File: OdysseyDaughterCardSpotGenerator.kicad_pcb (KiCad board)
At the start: 2 copper layers, 37.1 x 46.6 mm, 20 parts, among them Q1 2N3904, Q2 2N3904, Q3 BC547C, Q4 2N3904, X1 OdysseyDaughterCard

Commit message: 1.0 add port for emulator team
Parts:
- added J1: Conn_01x03, Connector_PinHeader_2.54mm:PinHeader_1x03_P2.54mm_Vertical, F.Cu at (156.7, 120.9)
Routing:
- net /Card9: track 8.65 -> 62.4 mm
- net /Card2: track 8.22 -> 29.7 mm
- net GND: track 57.5 -> 65.2 mm
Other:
- board text added: "Daughter Card Spot Generator 9-29-2018 r1.0 University of Pittsburgh Odyssey Restoration Project"
- board text removed: "Daughter Card Spot Generator 6-3-2018 r0.1 University of Pittsburgh Odyssey Restoration Project"
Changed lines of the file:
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@@
-(kicad_pcb (version 20171130) (host pcbnew "(2017-12-21 revision 23d71cfa9)-makepkg")
+(kicad_pcb (version 20171130) (host pcbnew "(5.0.0)")
   (general
     (thickness 1.6)
     (drawings 13)
-    (tracks 104)
+    (tracks 115)
     (zones 0)
-    (modules 20)
+    (modules 21)
     (nets 17)
   )
@@
   (title_block
     (title "Odyssey Daughter Card Spot Generator")
-    (date 2018-06-03)
-    (rev 0.1)
+    (date 2018-09-29)
+    (rev 1.0)
     (company "University of Pittsburgh - Odyssey Restoration Project")
     (comment 1 "Levi Burner")
@@
     (pcbplotparams
       (layerselection 0x010f0_ffffffff)
-      (usegerberextensions true)
+      (usegerberextensions false)
       (usegerberattributes false)
       (usegerberadvancedattributes false)
@@
       (hpglpennumber 1)
       (hpglpenspeed 20)
-      (hpglpendiameter 15)
+      (hpglpendiameter 15.000000)
       (psnegative false)
       (psa4output false)
@@
       (drillshape 0)
       (scaleselection 1)
-      (outputdirectory gerbers/))
+      (outputdirectory "gerbers/"))
   )
   (net 0 "")
@@
     )
   )
+  (module Connector_PinHeader_2.54mm:PinHeader_1x03_P2.54mm_Vertical (layer F.Cu)
+    (at 156.718 120.904 180)
+    (descr "Through hole straight pin header, 1x03, 2.54mm pitch, single row")
+    (tags "Through hole pin header THT 1x03 2.54mm single row")
+    (fp_text reference J1 (at 0 -2.33 180) (layer F.SilkS)
+      (effects (font (size 1 1) (thickness 0.15)))
+    )
+    (fp_text value Conn_01x03 (at 0 7.41 180) (layer F.Fab)
+      (effects (font (size 1 1) (thickness 0.15)))
+    )
+    (fp_line (start -0.635 -1.27) (end 1.27 -1.27) (layer F.Fab) (width 0.1))
+    (fp_line (start 1.27 -1.27) (end 1.27 6.35) (layer F.Fab) (width 0.1))
+    (fp_line (start 1.27 6.35) (end -1.27 6.35) (layer F.Fab) (width 0.1))
+    (fp_line (start -1.27 6.35) (end -1.27 -0.635) (layer F.Fab) (width 0.1))
+    (fp_line (start -1.27 -0.635) (end -0.635 -1.27) (layer F.Fab) (width 0.1))
+    (fp_line (start -1.33 6.41) (end 1.33 6.41) (layer F.SilkS) (width 0.12))
+    (fp_line (start -1.33 1.27) (end -1.33 6.41) (layer F.SilkS) (width 0.12))
+    (fp_line (start 1.33 1.27) (end 1.33 6.41) (layer F.SilkS) (width 0.12))
+    (fp_line (start -1.33 1.27) (end 1.33 1.27) (layer F.SilkS) (width 0.12))
+    (fp_line (start -1.33 0) (end -1.33 -1.33) (layer F.SilkS) (width 0.12))
+    (fp_line (start -1.33 -1.33) (end 0 -1.33) (layer F.SilkS) (width 0.12))
+    (fp_line (start -1.8 -1.8) (end -1.8 6.85) (layer F.CrtYd) (width 0.05))
+    (fp_line (start -1.8 6.85) (end 1.8 6.85) (layer F.CrtYd) (width 0.05))
+    (fp_line (start 1.8 6.85) (end 1.8 -1.8) (layer F.CrtYd) (width 0.05))
+    (fp_line (start 1.8 -1.8) (end -1.8 -1.8) (layer F.CrtYd) (width 0.05))
+    (fp_text user %R (at 0 2.54 270) (layer F.Fab)
+      (effects (font (size 1 1) (thickness 0.15)))
+    )
+    (pad 1 thru_hole rect (at 0 0 180) (size 1.7 1.7) (drill 1) (layers *.Cu *.Mask)
+      (net 16 /Card2))
+    (pad 2 thru_hole oval (at 0 2.54 180) (size 1.7 1.7) (drill 1) (layers *.Cu *.Mask)
+      (net 13 /Card9))
+    (pad 3 thru_hole oval (at 0 5.08 180) (size 1.7 1.7) (drill 1) (layers *.Cu *.Mask)
+      (net 11 GND))
+    (model ${KISYS3DMOD}/Connector_PinHeader_2.54mm.3dshapes/PinHeader_1x03_P2.54mm_Vertical.wrl
+      (at (xyz 0 0 0))
+      (scale (xyz 1 1 1))
+      (rotate (xyz 0 0 0))
+    )
+  )
   (gr_line (start 159.512 77.7) (end 159.512 124.3) (layer Edge.Cuts) (width 0.15))
   (gr_line (start 126.175 77.7) (end 122.425 77.7) (layer Edge.Cuts) (width 0.15))
@@
   (gr_line (start 126.175 124.3) (end 126.175 123.1) (layer Edge.Cuts) (width 0.15))
   (gr_line (start 122.425 124.3) (end 126.175 124.3) (layer Edge.Cuts) (width 0.15))
-  (gr_text "Daughter Card Spot Generator\n6-3-2018 r0.1\nUniversity of Pittsburgh\nOdyssey Restoration Project" (at 128.524 79.756 -90) (layer F.SilkS)
+  (gr_text "Daughter Card Spot Generator\n9-29-2018 r1.0\nUniversity of Pittsburgh\nOdyssey Restoration Project" (at 128.524 79.756 -90) (layer F.SilkS)
     (effects (font (size 1.2 1.2) (thickness 0.2)) (justify left))
   )
@@
   (segment (start 144.78 84.455) (end 144.78 80.812) (width 0.25) (layer B.Cu) (net 2))
   (segment (start 144.78 80.812) (end 144.78 80.772) (width 0.25) (layer B.Cu) (net 2))
-  (segment (start 148.8599 91.7823) (end 155.448 91.7823) (width 0.25) (layer F.Cu) (net 3))
-  (segment (start 145.9053 88.8277) (end 148.8599 91.7823) (width 0.25) (layer F.Cu) (net 3))
-  (segment (start 145.9053 88.265) (end 145.9053 88.8277) (width 0.25) (layer F.Cu) (net 3))
-  (segment (start 144.78 88.265) (end 145.9053 88.265) (width 0.25) (layer F.Cu) (net 3))
-  (segment (start 155.448 90.932) (end 155.448 91.7823) (width 0.25) (layer F.Cu) (net 3))
   (segment (start 155.956 92.2903) (end 155.956 99.608) (width 0.25) (layer B.Cu) (net 3))
   (segment (start 155.448 91.7823) (end 155.956 92.2903) (width 0.25) (layer B.Cu) (net 3))
   (segment (start 155.448 90.932) (end 155.448 91.7823) (width 0.25) (layer B.Cu) (net 3))
+  (segment (start 155.448 91.7823) (end 155.448 90.932) (width 0.25) (layer F.Cu) (net 3))
+  (segment (start 148.8599 91.7823) (end 155.448 91.7823) (width 0.25) (layer F.Cu) (net 3))
+  (segment (start 144.78 88.265) (end 145.3426 88.265) (width 0.25) (layer F.Cu) (net 3))
+  (segment (start 145.3426 88.265) (end 148.8599 91.7823) (width 0.25) (layer F.Cu) (net 3))
   (via (at 135.6058 94.3183) (size 0.8) (layers F.Cu B.Cu) (net 4))
   (segment (start 156.464 106.934) (end 155.3887 106.934) (width 0.25) (layer B.Cu) (net 4))
@@
   (segment (start 150.368 109.0543) (end 147.4501 111.9722) (width 0.25) (layer B.Cu) (net 11))
   (segment (start 150.368 108.204) (end 150.368 109.0543) (width 0.25) (layer B.Cu) (net 11))
+  (segment (start 156.718 108.458) (end 156.464 108.204) (width 0.25) (layer B.Cu) (net 11))
+  (segment (start 156.718 115.824) (end 156.718 108.458) (width 0.25) (layer B.Cu) (net 11))
   (segment (start 156.464 105.664) (end 150.368 105.664) (width 0.25) (layer F.Cu) (net 12))
   (segment (start 136.0347 104.4038) (end 134.8253 103.1944) (width 0.25) (layer B.Cu) (net 12))
@@
   (segment (start 137.16 84.455) (end 136.0092 84.455) (width 0.25) (layer B.Cu) (net 13))
   (segment (start 129 85.6389) (end 134.8253 85.6389) (width 0.25) (layer B.Cu) (net 13))
+  (segment (start 138.29137 84.455) (end 137.16 84.455) (width 0.25) (layer F.Cu) (net 13))
+  (segment (start 139.827 84.455) (end 138.29137 84.455) (width 0.25) (layer F.Cu) (net 13))
+  (segment (start 142.24 86.868) (end 139.827 84.455) (width 0.25) (layer F.Cu) (net 13))
+  (segment (start 157.893001 86.868) (end 142.24 86.868) (width 0.25) (layer F.Cu) (net 13))
+  (segment (start 156.718 118.364) (end 157.893001 117.188999) (width 0.25) (layer F.Cu) (net 13))
+  (segment (start 157.893001 117.188999) (end 157.893001 86.868) (width 0.25) (layer F.Cu) (net 13))
   (segment (start 137.16 88.265) (end 137.16 92.075) (width 0.25) (layer B.Cu) (net 14))
   (segment (start 137.16 92.075) (end 137.16 95.885) (width 0.25) (layer B.Cu) (net 14))
@@
   (segment (start 137.16 116.205) (end 134.9814 116.205) (width 0.25) (layer B.Cu) (net 16))
   (segment (start 129 116.3611) (end 134.8253 116.3611) (width 0.25) (layer B.Cu) (net 16))
+  (segment (start 155.618 120.904) (end 156.718 120.904) (width 0.25) (layer B.Cu) (net 16))
+  (segment (start 147.175001 120.904) (end 155.618 120.904) (width 0.25) (layer B.Cu) (net 16))
+  (segment (start 142.476001 116.205) (end 147.175001 120.904) (width 0.25) (layer B.Cu) (net 16))
+  (segment (start 137.16 116.205) (end 142.476001 116.205) (width 0.25) (layer B.Cu) (net 16))
 )

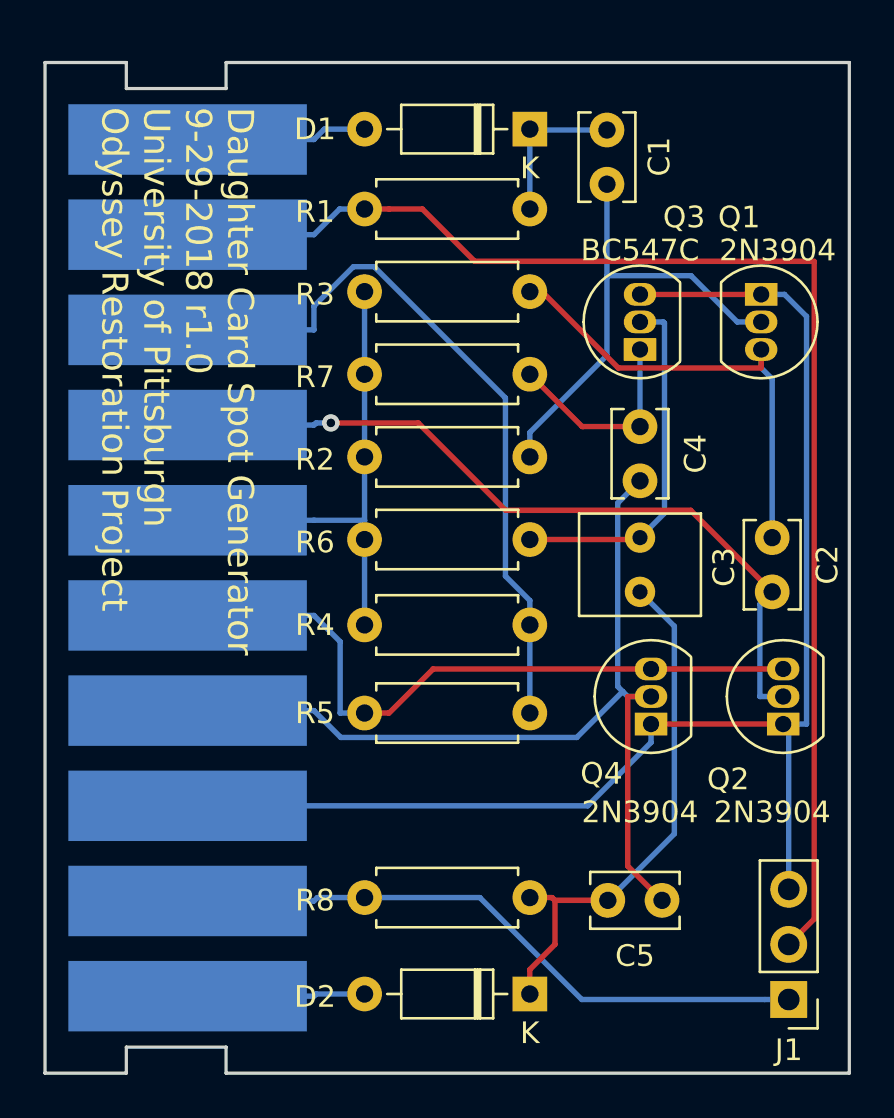
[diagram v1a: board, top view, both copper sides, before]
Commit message: R1.1 add header for extra player gen
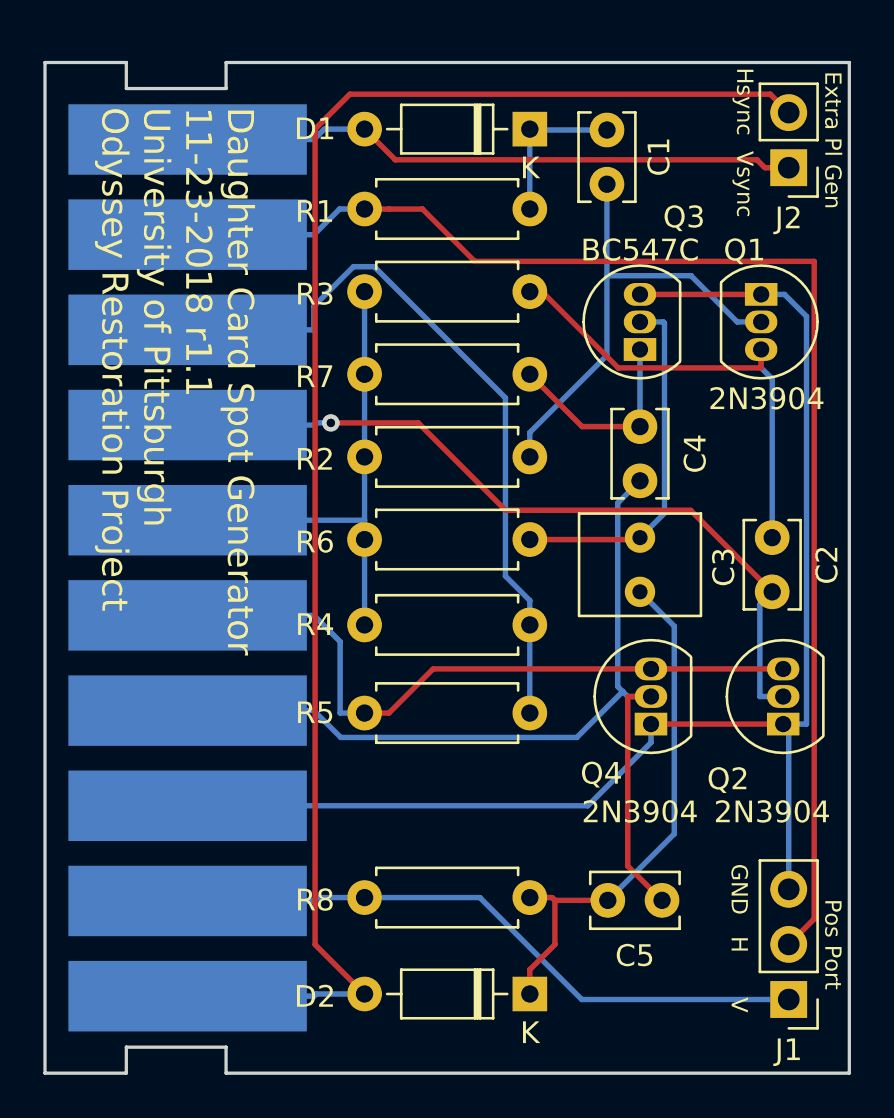
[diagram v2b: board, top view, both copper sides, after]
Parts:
- added J2: Conn_01x02, Connector_PinHeader_2.54mm:PinHeader_1x02_P2.54mm_Vertical, F.Cu at (156.7, 82.5)
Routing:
- net /Card1: track 8.20 -> 71.9 mm
- net /Card10: track 8.36 -> 28.7 mm
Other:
- board text added: "Daughter Card Spot Generator 11-23-2018 r1.1 University of Pittsburgh Odyssey Restoration Project"
- board text added: "Extra Pl Gen"
- board text added: "GND"
- board text added: "H"
- board text added: "Hsync"
- board text added: "Pos Port"
- board text added: "V"
- board text added: "Vsync"
- board text removed: "Daughter Card Spot Generator 9-29-2018 r1.0 University of Pittsburgh Odyssey Restoration Project"
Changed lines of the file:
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@@
-(kicad_pcb (version 20171130) (host pcbnew "(5.0.0)")
+(kicad_pcb (version 20171130) (host pcbnew "(5.0.1)-3")
   (general
     (thickness 1.6)
-    (drawings 13)
-    (tracks 115)
+    (drawings 20)
+    (tracks 124)
     (zones 0)
-    (modules 21)
+    (modules 22)
     (nets 17)
   )
@@
   (title_block
     (title "Odyssey Daughter Card Spot Generator")
-    (date 2018-09-29)
-    (rev 1.0)
+    (date 2018-11-23)
+    (rev 1.1)
     (company "University of Pittsburgh - Odyssey Restoration Project")
     (comment 1 "Levi Burner")
@@
     (pad_drill 0.762)
     (pad_to_mask_clearance 0.2)
+    (solder_mask_min_width 0.25)
     (aux_axis_origin 0 0)
     (visible_elements 7FFFFFFF)
@@
     (descr "TO-92 leads in-line, narrow, oval pads, drill 0.75mm (see NXP sot054_po.pdf)")
     (tags "to-92 sc-43 sc-43a sot54 PA33 transistor")
-    (fp_text reference Q1 (at -3.556 1.016) (layer F.SilkS)
-      (effects (font (size 1 1) (thickness 0.15)))
-    )
-    (fp_text value 2N3904 (at -2.032 -0.762) (layer F.SilkS)
+    (fp_text reference Q1 (at -2.032 0.762) (layer F.SilkS)
+      (effects (font (size 1 1) (thickness 0.15)))
+    )
+    (fp_text value 2N3904 (at 4.826 -0.254) (layer F.SilkS)
       (effects (font (size 1 1) (thickness 0.15)))
     )
@@
     )
   )
+  (module Connector_PinHeader_2.54mm:PinHeader_1x02_P2.54mm_Vertical (layer F.Cu)
+    (at 156.718 82.55 180)
+    (descr "Through hole straight pin header, 1x02, 2.54mm pitch, single row")
+    (tags "Through hole pin header THT 1x02 2.54mm single row")
+    (fp_text reference J2 (at 0 -2.33 180) (layer F.SilkS)
+      (effects (font (size 1 1) (thickness 0.15)))
+    )
+    (fp_text value Conn_01x02 (at 0 4.87 180) (layer F.Fab)
+      (effects (font (size 1 1) (thickness 0.15)))
+    )
+    (fp_line (start -0.635 -1.27) (end 1.27 -1.27) (layer F.Fab) (width 0.1))
+    (fp_line (start 1.27 -1.27) (end 1.27 3.81) (layer F.Fab) (width 0.1))
+    (fp_line (start 1.27 3.81) (end -1.27 3.81) (layer F.Fab) (width 0.1))
+    (fp_line (start -1.27 3.81) (end -1.27 -0.635) (layer F.Fab) (width 0.1))
+    (fp_line (start -1.27 -0.635) (end -0.635 -1.27) (layer F.Fab) (width 0.1))
+    (fp_line (start -1.33 3.87) (end 1.33 3.87) (layer F.SilkS) (width 0.12))
+    (fp_line (start -1.33 1.27) (end -1.33 3.87) (layer F.SilkS) (width 0.12))
+    (fp_line (start 1.33 1.27) (end 1.33 3.87) (layer F.SilkS) (width 0.12))
+    (fp_line (start -1.33 1.27) (end 1.33 1.27) (layer F.SilkS) (width 0.12))
+    (fp_line (start -1.33 0) (end -1.33 -1.33) (layer F.SilkS) (width 0.12))
+    (fp_line (start -1.33 -1.33) (end 0 -1.33) (layer F.SilkS) (width 0.12))
+    (fp_line (start -1.8 -1.8) (end -1.8 4.35) (layer F.CrtYd) (width 0.05))
+    (fp_line (start -1.8 4.35) (end 1.8 4.35) (layer F.CrtYd) (width 0.05))
+    (fp_line (start 1.8 4.35) (end 1.8 -1.8) (layer F.CrtYd) (width 0.05))
+    (fp_line (start 1.8 -1.8) (end -1.8 -1.8) (layer F.CrtYd) (width 0.05))
+    (fp_text user %R (at 0 1.27 270) (layer F.Fab)
+      (effects (font (size 1 1) (thickness 0.15)))
+    )
+    (pad 1 thru_hole rect (at 0 0 180) (size 1.7 1.7) (drill 1) (layers *.Cu *.Mask)
+      (net 9 /Card10))
+    (pad 2 thru_hole oval (at 0 2.54 180) (size 1.7 1.7) (drill 1) (layers *.Cu *.Mask)
+      (net 10 /Card1))
+    (model ${KISYS3DMOD}/Connector_PinHeader_2.54mm.3dshapes/PinHeader_1x02_P2.54mm_Vertical.wrl
+      (at (xyz 0 0 0))
+      (scale (xyz 1 1 1))
+      (rotate (xyz 0 0 0))
+    )
+  )
+  (gr_text Vsync (at 154.686 83.312 270) (layer F.SilkS)
+    (effects (font (size 0.75 0.75) (thickness 0.1)))
+  )
+  (gr_text Hsync (at 154.686 79.502 270) (layer F.SilkS)
+    (effects (font (size 0.75 0.75) (thickness 0.1)))
+  )
+  (gr_text "Extra Pl Gen" (at 158.75 81.28 270) (layer F.SilkS)
+    (effects (font (size 0.75 0.75) (thickness 0.1)))
+  )
+  (gr_text V (at 154.432 121.158 270) (layer F.SilkS)
+    (effects (font (size 0.75 0.75) (thickness 0.1)))
+  )
+  (gr_text H (at 154.432 118.364 270) (layer F.SilkS)
+    (effects (font (size 0.75 0.75) (thickness 0.1)))
+  )
+  (gr_text GND (at 154.432 115.824 270) (layer F.SilkS)
+    (effects (font (size 0.75 0.75) (thickness 0.1)))
+  )
+  (gr_text "Pos Port" (at 158.75 118.364 270) (layer F.SilkS)
+    (effects (font (size 0.75 0.75) (thickness 0.1)))
+  )
   (gr_line (start 159.512 77.7) (end 159.512 124.3) (layer Edge.Cuts) (width 0.15))
   (gr_line (start 126.175 77.7) (end 122.425 77.7) (layer Edge.Cuts) (width 0.15))
@@
   (gr_line (start 126.175 124.3) (end 126.175 123.1) (layer Edge.Cuts) (width 0.15))
   (gr_line (start 122.425 124.3) (end 126.175 124.3) (layer Edge.Cuts) (width 0.15))
-  (gr_text "Daughter Card Spot Generator\n9-29-2018 r1.0\nUniversity of Pittsburgh\nOdyssey Restoration Project" (at 128.524 79.756 -90) (layer F.SilkS)
+  (gr_text "Daughter Card Spot Generator\n11-23-2018 r1.1\nUniversity of Pittsburgh\nOdyssey Restoration Project" (at 128.524 79.756 -90) (layer F.SilkS)
     (effects (font (size 1.2 1.2) (thickness 0.2)) (justify left))
   )
@@
   (segment (start 137.16 80.772) (end 135.3033 80.772) (width 0.25) (layer B.Cu) (net 9))
   (segment (start 129 81.25) (end 134.8253 81.25) (width 0.25) (layer B.Cu) (net 9))
+  (segment (start 155.618 82.55) (end 156.718 82.55) (width 0.25) (layer F.Cu) (net 9))
+  (segment (start 155.254999 82.186999) (end 155.618 82.55) (width 0.25) (layer F.Cu) (net 9))
+  (segment (start 138.574999 82.186999) (end 155.254999 82.186999) (width 0.25) (layer F.Cu) (net 9))
+  (segment (start 137.16 80.772) (end 138.574999 82.186999) (width 0.25) (layer F.Cu) (net 9))
   (segment (start 134.9253 120.65) (end 134.8253 120.75) (width 0.25) (layer B.Cu) (net 10))
   (segment (start 137.16 120.65) (end 134.9253 120.65) (width 0.25) (layer B.Cu) (net 10))
   (segment (start 129 120.75) (end 134.8253 120.75) (width 0.25) (layer B.Cu) (net 10))
+  (segment (start 134.880799 118.370799) (end 134.880799 80.765201) (width 0.25) (layer F.Cu) (net 10))
+  (segment (start 137.16 120.65) (end 134.880799 118.370799) (width 0.25) (layer F.Cu) (net 10))
+  (segment (start 155.868001 79.160001) (end 156.718 80.01) (width 0.25) (layer F.Cu) (net 10))
+  (segment (start 136.485999 79.160001) (end 155.868001 79.160001) (width 0.25) (layer F.Cu) (net 10))
+  (segment (start 134.880799 80.765201) (end 136.485999 79.160001) (width 0.25) (layer F.Cu) (net 10))
   (segment (start 149.86 88.392) (end 155.448 88.392) (width 0.25) (layer F.Cu) (net 11))
   (segment (start 156.464 108.204) (end 150.368 108.204) (width 0.25) (layer F.Cu) (net 11))
